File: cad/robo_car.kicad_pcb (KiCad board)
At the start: 2 copper layers, 100 x 100 mm, 88 parts, among them J1 Conn_01x06_MountingPin, J16 Conn_01x02_MountingPin, J2 ftdi_conn, J3 Conn_01x06_MountingPin, J4 Conn_01x04, J5 Conn_01x04, J6 Conn_01x06_MountingPin, J7 Conn_01x02_MountingPin, J8 Conn_01x02_MountingPin, SW1 SW_Push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

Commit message: More awake Olivia fixes some things
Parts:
- removed C16: 47uF, Capacitor_SMD:CP_Elec_6.3x7.7
- moved D15 4.60 mm to (166.9, 119.7)
- moved R10 4.52 mm to (166.9, 123.3)
- moved R9 3.82 mm to (163.9, 123.4)
- moved D14 3.78 mm to (163.9, 119.7)
- moved R8 2.89 mm to (160.9, 123.4)
- moved D13 2.77 mm to (160.9, 119.7)
- moved D12 1.93 mm to (158.1, 119.8)
- moved R4 1.93 mm to (158.0, 123.4)
- moved J2 0.86 mm to (142.6, 144.4)
- moved C22 0.17 mm to (164.8, 79.7)
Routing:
- net /INPUT_D: track 0.00 -> 89.7 mm, vias 0 -> 6
- net /VREG_OUT: track 82.0 -> 161.2 mm, vias 2 -> 8
- net /NEO_STATUS: track 0.00 -> 55.0 mm, vias 0 -> 4
- net +3V3: track 216.5 -> 266.7 mm, vias 2 -> 6
- net /HBT_LED: track 0.00 -> 39.1 mm, vias 0 -> 4
- net /MOTOR_L_2: track 5.67 -> 40.6 mm
- net /MOTOR_R_2: track 10.9 -> 45.4 mm
- net /MOTOR_R_1: track 8.40 -> 42.7 mm
- net /MOTOR_L_1: track 2.61 -> 35.5 mm
- net /CAN_RX: track 0.00 -> 30.9 mm, vias 0 -> 4
- net /BOOT: track 0.00 -> 28.0 mm, vias 0 -> 2
- net VBUS: track 51.3 -> 78.2 mm, vias 18 -> 20
- net /CAN_TX: track 0.00 -> 17.2 mm, vias 0 -> 2
- net /NEO_BAR: track 107.2 -> 105.8 mm, vias 0 -> 2
- net /TXDO: track 7.84 -> 8.72 mm
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
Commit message: lots of vias, maybe too much?
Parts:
- moved G*** 1.54 mm to (150.8, 102.4)
- moved G*** 1.52 mm to (150.9, 101.1)
- moved SW2 1.05 mm to (182.1, 147.6)
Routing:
- net /NEO_BAR: track 105.8 -> 63.2 mm, vias 2 -> 0
- net /NEO_STATUS: track 55.0 -> 38.2 mm
- net /CAN_RX: track 30.9 -> 25.3 mm, vias 4 -> 2
- net /BOOT: track 28.0 -> 23.2 mm
- net +3V3: track 266.7 -> 270.7 mm
- net /RESET: track 39.7 -> 40.3 mm
- net /VREG_OUT: vias 8 -> 6
- net GND: vias 16 -> 535
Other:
- board text added: "Reset"
- board text added: "Roger"
- board text removed: "^ Reset :)"

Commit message: Little tiny baby commit where i push the little tiny baby changes
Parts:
- moved G*** 0.18 mm to (150.8, 101.3)
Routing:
- net /VREG_OUT: track 161.2 -> 141.6 mm
- net +3V3: track 270.7 -> 268.6 mm
- net /HBT_LED: track 39.1 -> 37.5 mm, vias 4 -> 2
- net /INPUT_D: track 89.7 -> 90.4 mm, vias 6 -> 4
- net /FUNCTION_BUTTON: track 50.1 -> 50.0 mm, vias 2 -> 0
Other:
- board text added: "A"
- board text added: "B"
- board text added: "C"
- board text added: "D"

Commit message: Big Kahuna finished, winrar zippy files are funny
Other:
- board text added: "15"
- board text added: "25"
- board text added: "26"
- board text added: "33"
- board text added: "INPUT ONLY"
- board text added: "RX 16"
- board text added: "TX 4"
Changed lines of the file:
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@@
       ) (layer "B.SilkS") (width 0) (fill solid))
   )
-  (gr_line (start 147.625 69.23) (end 145.125 69.23) (layer "F.SilkS") (width 0.12))
   (gr_rect (start 189.925 82.905) (end 174.925 80.405) (layer "F.SilkS") (width 0.12) (fill none))
   (gr_line (start 182.44 82.85) (end 182.44 85.35) (layer "F.SilkS") (width 0.12))
@@
   (gr_line (start 179.925 82.905) (end 179.925 80.405) (layer "F.SilkS") (width 0.12))
   (gr_line (start 184.925 80.405) (end 182.425 80.405) (layer "F.SilkS") (width 0.12))
-  (gr_line (start 150.125 71.73) (end 150.125 69.23) (layer "F.SilkS") (width 0.12))
+  (gr_line (start 120.67 84.49) (end 120.67 81.99) (layer "F.SilkS") (width 0.12))
+  (gr_line (start 150.46 71.56) (end 150.46 69.06) (layer "F.SilkS") (width 0.12))
+  (gr_line (start 150.53 71.39) (end 150.53 73.89) (layer "F.SilkS") (width 0.12))
   (gr_line (start 123.175 79.555) (end 123.175 82.055) (layer "F.SilkS") (width 0.12))
   (gr_line (start 177.425 80.405) (end 177.425 82.905) (layer "F.SilkS") (width 0.12))
-  (gr_line (start 155.125 71.73) (end 152.625 71.73) (layer "F.SilkS") (width 0.12))
+  (gr_rect (start 125.68 84.49) (end 115.64 82.03) (layer "F.SilkS") (width 0.12) (fill none))
   (gr_line (start 187.44 85.36) (end 187.44 82.86) (layer "F.SilkS") (width 0.12))
+  (gr_line (start 155.53 73.9) (end 155.53 71.4) (layer "F.SilkS") (width 0.12))
   (gr_line (start 184.92 85.36) (end 184.92 82.86) (layer "F.SilkS") (width 0.12))
+  (gr_line (start 118.19 81.98) (end 118.19 84.48) (layer "F.SilkS") (width 0.12))
   (gr_line (start 187.425 80.405) (end 187.425 82.905) (layer "F.SilkS") (width 0.12))
   (gr_rect (start 125.675 82.055) (end 110.675 79.555) (layer "F.SilkS") (width 0.12) (fill none))
-  (gr_line (start 145.125 69.23) (end 145.125 71.73) (layer "F.SilkS") (width 0.12))
-  (gr_line (start 152.625 69.23) (end 150.125 69.23) (layer "F.SilkS") (width 0.12))
-  (gr_rect (start 157.625 71.73) (end 142.625 69.23) (layer "F.SilkS") (width 0.12) (fill none))
+  (gr_line (start 145.46 69.06) (end 145.46 71.56) (layer "F.SilkS") (width 0.12))
+  (gr_rect (start 157.96 71.56) (end 142.96 69.06) (layer "F.SilkS") (width 0.12) (fill none))
   (gr_line (start 118.175 82.055) (end 118.175 79.555) (layer "F.SilkS") (width 0.12))
   (gr_line (start 115.675 79.555) (end 113.175 79.555) (layer "F.SilkS") (width 0.12))
   (gr_line (start 187.425 82.905) (end 184.925 82.905) (layer "F.SilkS") (width 0.12))
-  (gr_line (start 152.625 71.73) (end 152.625 69.23) (layer "F.SilkS") (width 0.12))
+  (gr_line (start 152.96 71.56) (end 152.96 69.06) (layer "F.SilkS") (width 0.12))
   (gr_line (start 120.675 82.055) (end 120.675 79.555) (layer "F.SilkS") (width 0.12))
   (gr_line (start 115.675 82.055) (end 115.675 79.555) (layer "F.SilkS") (width 0.12))
   (gr_line (start 113.175 79.555) (end 113.175 82.055) (layer "F.SilkS") (width 0.12))
   (gr_rect (start 189.93 85.36) (end 179.89 82.9) (layer "F.SilkS") (width 0.12) (fill none))
+  (gr_line (start 123.19 84.49) (end 123.19 81.99) (layer "F.SilkS") (width 0.12))
+  (gr_rect (start 158.02 73.9) (end 147.98 71.44) (layer "F.SilkS") (width 0.12) (fill none))
   (gr_line (start 179.925 80.405) (end 177.425 80.405) (layer "F.SilkS") (width 0.12))
-  (gr_line (start 155.125 69.23) (end 155.125 71.73) (layer "F.SilkS") (width 0.12))
+  (gr_line (start 155.46 69.06) (end 155.46 71.56) (layer "F.SilkS") (width 0.12))
   (gr_line (start 182.425 82.905) (end 182.425 80.405) (layer "F.SilkS") (width 0.12))
   (gr_line (start 123.175 82.055) (end 120.675 82.055) (layer "F.SilkS") (width 0.12))
-  (gr_line (start 147.625 71.73) (end 147.625 69.23) (layer "F.SilkS") (width 0.12))
+  (gr_line (start 147.96 71.56) (end 147.96 69.06) (layer "F.SilkS") (width 0.12))
+  (gr_line (start 153.01 73.9) (end 153.01 71.4) (layer "F.SilkS") (width 0.12))
   (gr_line (start 184.925 82.905) (end 184.925 80.405) (layer "F.SilkS") (width 0.12))
   (gr_circle (center 105.01 89.99) (end 106.61 89.99) (layer "Eco2.User") (width 0.4) (fill none))
@@
     (effects (font (size 1 1) (thickness 0.25)))
   )
+  (gr_text "B" (at 119.44 83.26) (layer "F.SilkS")
+    (effects (font (size 1 1) (thickness 0.15)))
+  )
   (gr_text "3" (at 158.75 88.305) (layer "F.SilkS")
     (effects (font (size 1 1) (thickness 0.25)))
   )
-  (gr_text "18" (at 154.025 70.505) (layer "F.SilkS")
+  (gr_text "18" (at 154.36 70.335) (layer "F.SilkS")
     (effects (font (size 1 1) (thickness 0.15)))
   )
   (gr_text "35" (at 183.75 81.705) (layer "F.SilkS")
+    (effects (font (size 1 1) (thickness 0.15)))
+  )
+  (gr_text "A" (at 149.43 72.7) (layer "F.SilkS")
     (effects (font (size 1 1) (thickness 0.15)))
   )
@@
     (effects (font (size 1.5 1.5) (thickness 0.3)))
   )
-  (gr_text "17" (at 148.975 70.555) (layer "F.SilkS")
-    (effects (font (size 1 1) (thickness 0.15)))
+  (gr_text "17" (at 149.31 70.385) (layer "F.SilkS")
+    (effects (font (size 1 1) (thickness 0.15)))
+  )
+  (gr_text "25" (at 163.66 117.47) (layer "F.SilkS")
+    (effects (font (size 1 1) (thickness 0.25)))
   )
   (gr_text "Button" (at 193.852 106.448) (layer "F.SilkS")
     (effects (font (size 1 1) (thickness 0.15)))
   )
-  (gr_text "3V" (at 146.425 70.555) (layer "F.SilkS")
+  (gr_text "3V" (at 146.76 70.385) (layer "F.SilkS")
     (effects (font (size 1 1) (thickness 0.15)))
   )
@@
     (effects (font (size 1 1) (thickness 0.15)))
   )
+  (gr_text "INPUT ONLY" (at 182.12 69.69) (layer "F.SilkS")
+    (effects (font (size 1.5 1.5) (thickness 0.3)))
+  )
+  (gr_text "26" (at 160.6 117.52) (layer "F.SilkS")
+    (effects (font (size 1 1) (thickness 0.25)))
+  )
   (gr_text "4" (at 165.608 88.33) (layer "F.SilkS")
     (effects (font (size 1 1) (thickness 0.25)))
   )
+  (gr_text "33" (at 166.52 117.47) (layer "F.SilkS")
+    (effects (font (size 1 1) (thickness 0.25)))
+  )
+  (gr_text "D" (at 156.7 72.7) (layer "F.SilkS")
+    (effects (font (size 1 1) (thickness 0.15)))
+  )
   (gr_text "12" (at 177 108.204) (layer "F.SilkS")
     (effects (font (size 1 1) (thickness 0.15)))
@@
     (effects (font (size 1 1) (thickness 0.15)))
   )
+  (gr_text "RX 16" (at 135.32 128.88) (layer "F.SilkS")
+    (effects (font (size 1 1) (thickness 0.25)))
+  )
+  (gr_text "D" (at 124.36 83.29) (layer "F.SilkS")
+    (effects (font (size 1 1) (thickness 0.15)))
+  )
   (gr_text "Function" (at 193.802 104.648) (layer "F.SilkS")
     (effects (font (size 1 1) (thickness 0.15)))
   )
-  (gr_text "G" (at 143.875 70.53) (layer "F.SilkS")
+  (gr_text "G" (at 144.21 70.36) (layer "F.SilkS")
     (effects (font (size 1 1) (thickness 0.15)))
   )
@@
     (effects (font (size 1 1) (thickness 0.15)))
   )
-  (gr_text "5" (at 151.45 70.53) (layer "F.SilkS")
+  (gr_text "5" (at 151.785 70.36) (layer "F.SilkS")
     (effects (font (size 1 1) (thickness 0.15)))
   )
@@
   )
   (gr_text "5V" (at 182.626 88.392) (layer "F.SilkS")
+    (effects (font (size 1 1) (thickness 0.15)))
+  )
+  (gr_text "C" (at 121.96 83.26) (layer "F.SilkS")
     (effects (font (size 1 1) (thickness 0.15)))
   )
@@
     (effects (font (size 1.3 1.3) (thickness 0.15)))
   )
+  (gr_text "TX 4" (at 135.28 135.41) (layer "F.SilkS")
+    (effects (font (size 1 1) (thickness 0.25)))
+  )
   (gr_text "A" (at 181.34 84.16) (layer "F.SilkS")
     (effects (font (size 1 1) (thickness 0.15)))
@@
     (effects (font (size 1 1) (thickness 0.15)))
   )
+  (gr_text "12" (at 157.69 117.53) (layer "F.SilkS")
+    (effects (font (size 1 1) (thickness 0.25)))
+  )
+  (gr_text "15" (at 135.48 82.46) (layer "F.SilkS")
+    (effects (font (size 1 1) (thickness 0.25)))
+  )
   (gr_text "32" (at 181.275 81.73) (layer "F.SilkS")
     (effects (font (size 1 1) (thickness 0.15)))
   )
+  (gr_text "B" (at 151.78 72.67) (layer "F.SilkS")
+    (effects (font (size 1 1) (thickness 0.15)))
+  )
   (gr_text "21" (at 122.075 80.83) (layer "F.SilkS")
     (effects (font (size 1 1) (thickness 0.15)))
   )
+  (gr_text "C" (at 154.3 72.67) (layer "F.SilkS")
+    (effects (font (size 1 1) (thickness 0.15)))
+  )
   (gr_text "3V" (at 114.475 80.88) (layer "F.SilkS")
     (effects (font (size 1 1) (thickness 0.15)))
@@
     (effects (font (size 1 1) (thickness 0.15)))
   )
-  (gr_text "13" (at 156.4 70.53) (layer "F.SilkS")
+  (gr_text "13" (at 156.735 70.36) (layer "F.SilkS")
     (effects (font (size 1 1) (thickness 0.15)))
   )
@@
     (effects (font (size 1 1) (thickness 0.15)))
   )
+  (gr_text "A" (at 117.09 83.29) (layer "F.SilkS")
+    (effects (font (size 1 1) (thickness 0.15)))
+  )

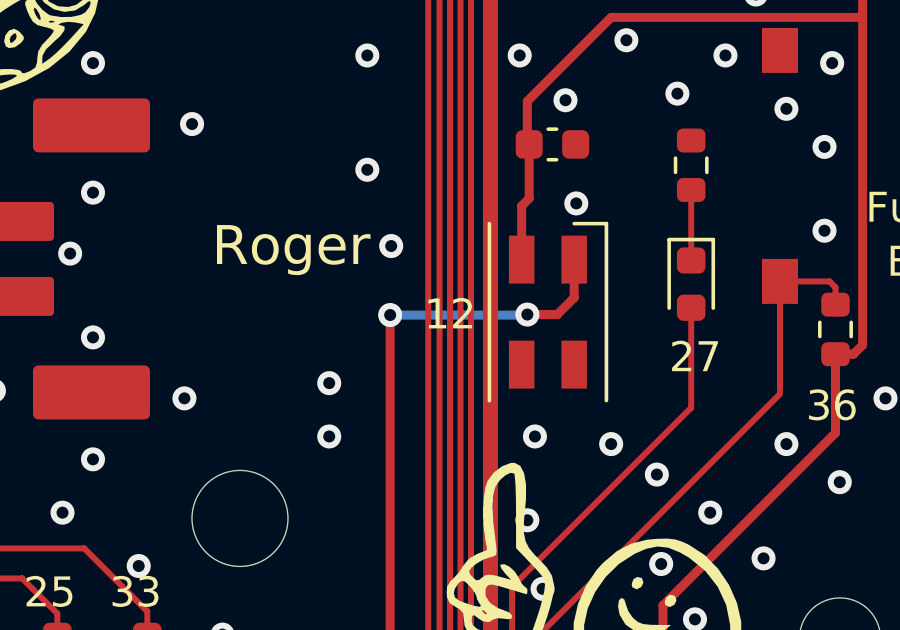
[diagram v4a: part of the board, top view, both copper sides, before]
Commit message: I fixed the label for the pin we changed cause bad label is bad
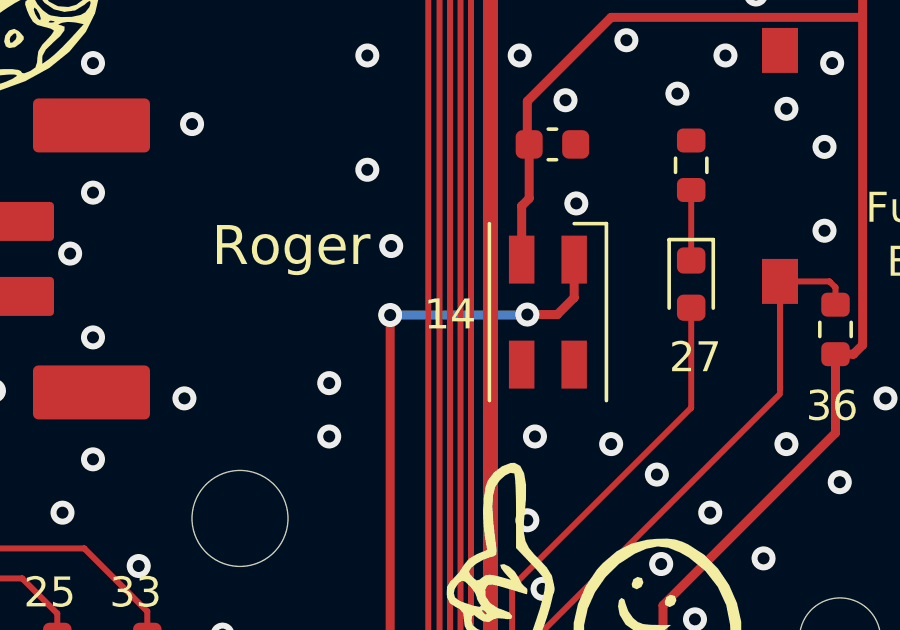
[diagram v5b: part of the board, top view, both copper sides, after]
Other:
- board text added: "14"
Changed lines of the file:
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@@
     (effects (font (size 1 1) (thickness 0.15)))
   )
-  (gr_text "12" (at 177 108.204) (layer "F.SilkS")
+  (gr_text "14" (at 177 108.204) (layer "F.SilkS")
     (effects (font (size 1 1) (thickness 0.15)))
   )
